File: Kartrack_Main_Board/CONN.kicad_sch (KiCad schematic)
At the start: 4 parts, among them J1 USB_C_Receptacle_USB2.0_14P

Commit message: schematic GPS
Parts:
- added JP1: SolderJumper_2_Open, symbol Jumper:SolderJumper_2_Open
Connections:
- net +3.3V: no longer A2.4 (3V3)
- net PC6 renamed PC6_TX
- net PC7 renamed PC7_RX
- net VDD: no longer names the net of A2.8 (VIN)
- net VDD: now also JP1.1 (A)
- new net VEXT_DISCO: JP1.2 (B)
- no-connect marks 4 -> 5
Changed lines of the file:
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@@
+	)
+	(no_connect
+		(at 191.77 66.04)
 	)
 	(no_connect
@@
 	(wire
 		(pts
-			(xy 186.69 57.15) (xy 186.69 66.04)
+			(xy 186.69 54.61) (xy 186.69 55.88)
 		)
 		(stroke
@@
 	(wire
 		(pts
+			(xy 186.69 63.5) (xy 186.69 66.04)
+		)
+		(stroke
+			(width 0)
+			(type default)
+		)
+	)
+	(wire
+		(pts
 			(xy 71.12 74.93) (xy 72.39 74.93)
 		)
@@
 	(wire
 		(pts
-			(xy 190.5 66.04) (xy 191.77 66.04)
-		)
-		(stroke
-			(width 0)
-			(type default)
-		)
-	)
-	(wire
-		(pts
 			(xy 71.12 80.01) (xy 77.47 80.01)
 		)
@@
 		)
 	)
-	(wire
-		(pts
-			(xy 190.5 66.04) (xy 190.5 63.5)
-		)
-		(stroke
-			(width 0)
-			(type default)
-		)
-	)
 	(hierarchical_label "PI1{slash}LD1"
 		(shape input)
@@
 		)
 	)
-	(hierarchical_label "PC6"
+	(hierarchical_label "PC6_TX"
 		(shape input)
 		(at 176.53 78.74 180)
@@
 		)
 	)
-	(hierarchical_label "PC7"
+	(hierarchical_label "PC7_RX"
 		(shape input)
 		(at 176.53 76.2 180)
@@
 	)
 	(symbol
-		(lib_id "power:+3.3V")
-		(at 190.5 63.5 0)
-		(unit 1)
-		(exclude_from_sim no)
-		(in_bom yes)
-		(on_board yes)
-		(dnp no)
-		(fields_autoplaced yes)
-		(property "Reference" "#PWR03"
-			(at 190.5 67.31 0)
-			(effects
-				(font
-					(size 1.27 1.27)
-				)
-				(hide yes)
-			)
-		)
-		(property "Value" "+3.3V"
-			(at 190.5 58.42 0)
-			(effects
-				(font
-					(size 1.27 1.27)
-				)
-			)
-		)
-		(property "Footprint" ""
-			(at 190.5 63.5 0)
-			(effects
-				(font
-					(size 1.27 1.27)
-				)
-				(hide yes)
-			)
-		)
-		(property "Datasheet" ""
-			(at 190.5 63.5 0)
-			(effects
-				(font
-					(size 1.27 1.27)
-				)
-				(hide yes)
-			)
-		)
-		(property "Description" "Power symbol creates a global label with name \"+3.3V\""
-			(at 190.5 63.5 0)
-			(effects
-				(font
-					(size 1.27 1.27)
-				)
-				(hide yes)
-			)
-		)
-		(pin "1"
-		)
-		(instances
-			(project "Kartrack_Main_Board"
-				(path "/7d0ecb76-dd3a-488e-b45e-ae217463e751/85ccdc23-ae17-49a7-b6f3-41d41d1b2e3d"
-					(reference "#PWR03")
-					(unit 1)
-				)
-			)
-		)
-	)
-	(symbol
 		(lib_id "power:VDD")
-		(at 186.69 57.15 0)
+		(at 186.69 54.61 0)
 		(unit 1)
 		(exclude_from_sim no)
@@
 		(fields_autoplaced yes)
 		(property "Reference" "#PWR04"
-			(at 186.69 60.96 0)
-			(effects
-				(font
-					(size 1.27 1.27)
-				)
-				(hide yes)
-			)
-		)
-		(property "Value" "VDD"
-			(at 186.69 52.07 0)
+			(at 186.69 58.42 0)
+			(effects
+				(font
+					(size 1.27 1.27)
+				)
+				(hide yes)
+			)
+		)
+		(property "Value" "VEXT_DISCO"
+			(at 186.69 49.53 0)
 			(effects
 				(font
@@
 		)
 		(property "Footprint" ""
-			(at 186.69 57.15 0)
+			(at 186.69 54.61 0)
 			(effects
 				(font
@@
 		)
 		(property "Datasheet" ""
-			(at 186.69 57.15 0)
+			(at 186.69 54.61 0)
 			(effects
 				(font
@@
 		)
 		(property "Description" "Power symbol creates a global label with name \"VDD\""
-			(at 186.69 57.15 0)
+			(at 186.69 54.61 0)
 			(effects
 				(font
@@
 					(unit 1)
 				)
+			)
+		)
+	)
+	(symbol
+		(lib_id "Jumper:SolderJumper_2_Open")
+		(at 186.69 59.69 90)
+		(unit 1)
+		(exclude_from_sim yes)
+		(in_bom no)
+		(on_board yes)
+		(dnp no)
+		(property "Reference" "JP1"
+			(at 173.736 57.912 90)
+			(effects
+				(font
+					(size 1.27 1.27)
+				)
+				(justify right)
+			)
+		)
+		(property "Value" "SolderJumper_2_Open"
+			(at 159.512 60.96 90)
+			(effects
+				(font
+					(size 1.27 1.27)
+				)
+				(justify right)
+			)
+		)
+		(property "Footprint" ""
+			(at 186.69 59.69 0)
+			(effects
+				(font
+					(size 1.27 1.27)
+				)
+				(hide yes)
+			)
+		)
+		(property "Datasheet" "~"
+			(at 186.69 59.69 0)
+			(effects
+				(font
+					(size 1.27 1.27)
+				)
+				(hide yes)
+			)
+		)
+		(property "Description" "Solder Jumper, 2-pole, open"
+			(at 186.69 59.69 0)
+			(effects
+				(font
+					(size 1.27 1.27)
+				)
+				(hide yes)
+			)
+		)
+		(pin "2"
+		)
+		(pin "1"
+		)
+		(instances
+			(project ""
+				(path "/7d0ecb76-dd3a-488e-b45e-ae217463e751/85ccdc23-ae17-49a7-b6f3-41d41d1b2e3d"
+					(reference "JP1")
+					(unit 1)
+				)

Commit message: BLOC schematic
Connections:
- net PB14 renamed PB14_SPI2_MISO
- net PB15 renamed PB15_SPI2_MOSI
- net PB8 renamed PB8_SCL
- net PB9 renamed PB9_SDA
- net PI1/LD1 renamed PI1_SPI2_SCK
- net PIO renamed PIO_SPI2_NSS
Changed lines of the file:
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@@
 		)
 	)
-	(hierarchical_label "PI1{slash}LD1"
+	(hierarchical_label "PI1_SPI2_SCK"
 		(shape input)
 		(at 176.53 109.22 180)
@@
 		)
 	)
-	(hierarchical_label "PB8"
+	(hierarchical_label "PB8_SCL"
 		(shape input)
 		(at 201.93 111.76 0)
@@
 		)
 	)
-	(hierarchical_label "PIO"
+	(hierarchical_label "PIO_SPI2_NSS"
 		(shape input)
 		(at 176.53 88.9 180)
@@
 		)
 	)
-	(hierarchical_label "PB15"
+	(hierarchical_label "PB15_SPI2_MOSI"
 		(shape input)
 		(at 176.53 104.14 180)
@@
 		)
 	)
-	(hierarchical_label "PB14"
+	(hierarchical_label "PB14_SPI2_MISO"
 		(shape input)
 		(at 176.53 106.68 180)
@@
 		)
 	)
-	(hierarchical_label "PB9"
+	(hierarchical_label "PB9_SDA"
 		(shape input)
 		(at 201.93 109.22 0)

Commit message: ajouts des boutons
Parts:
- added SW1, SW2, SW3: SW_Push, symbol Switch:SW_Push
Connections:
- net +3.3V: now also SW1.2, SW2.2, SW3.2
- net PA0: now also SW1.1
- net PF10: now also SW2.1
- net PF9: now also SW3.1

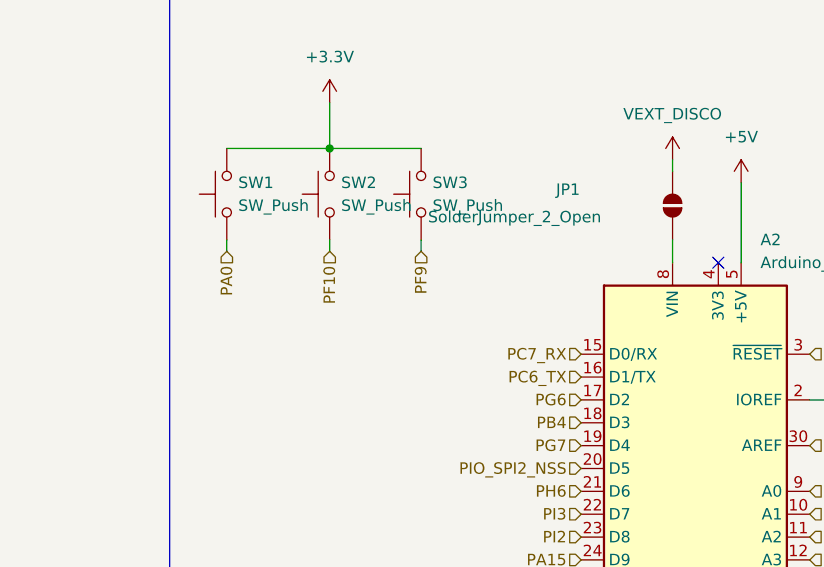
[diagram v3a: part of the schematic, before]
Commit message: added connectors for pulldown pushbuttons
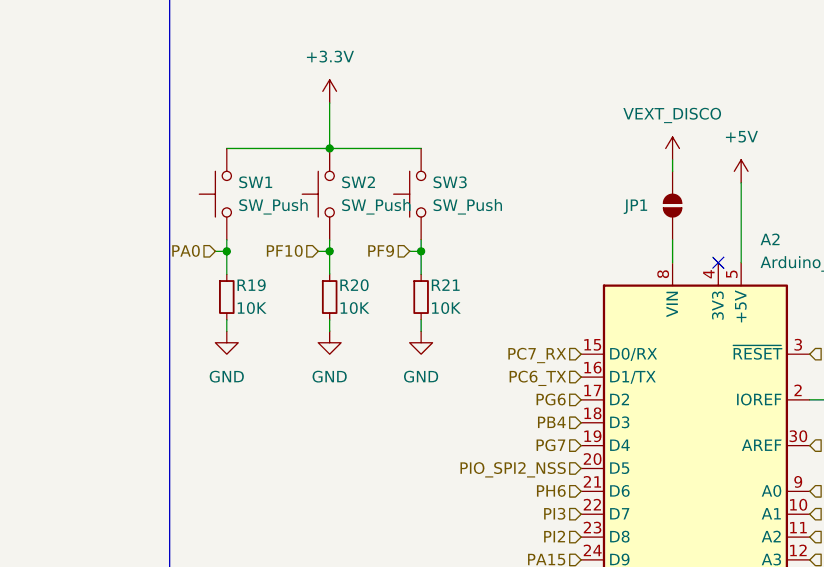
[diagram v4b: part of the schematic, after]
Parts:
- added R19, R20, R21: 10K, symbol Device:R_Small
- SW1, SW2, SW3: footprint (none) -> Connector_PinSocket_2.54mm:PinSocket_1x02_P2.54mm_Vertical_SMD_Pin1Left
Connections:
- net GND: now also R19.2, R20.2, R21.2
- net PA0: now also R19.1
- net PF10: now also R20.1
- net PF9: now also R21.1

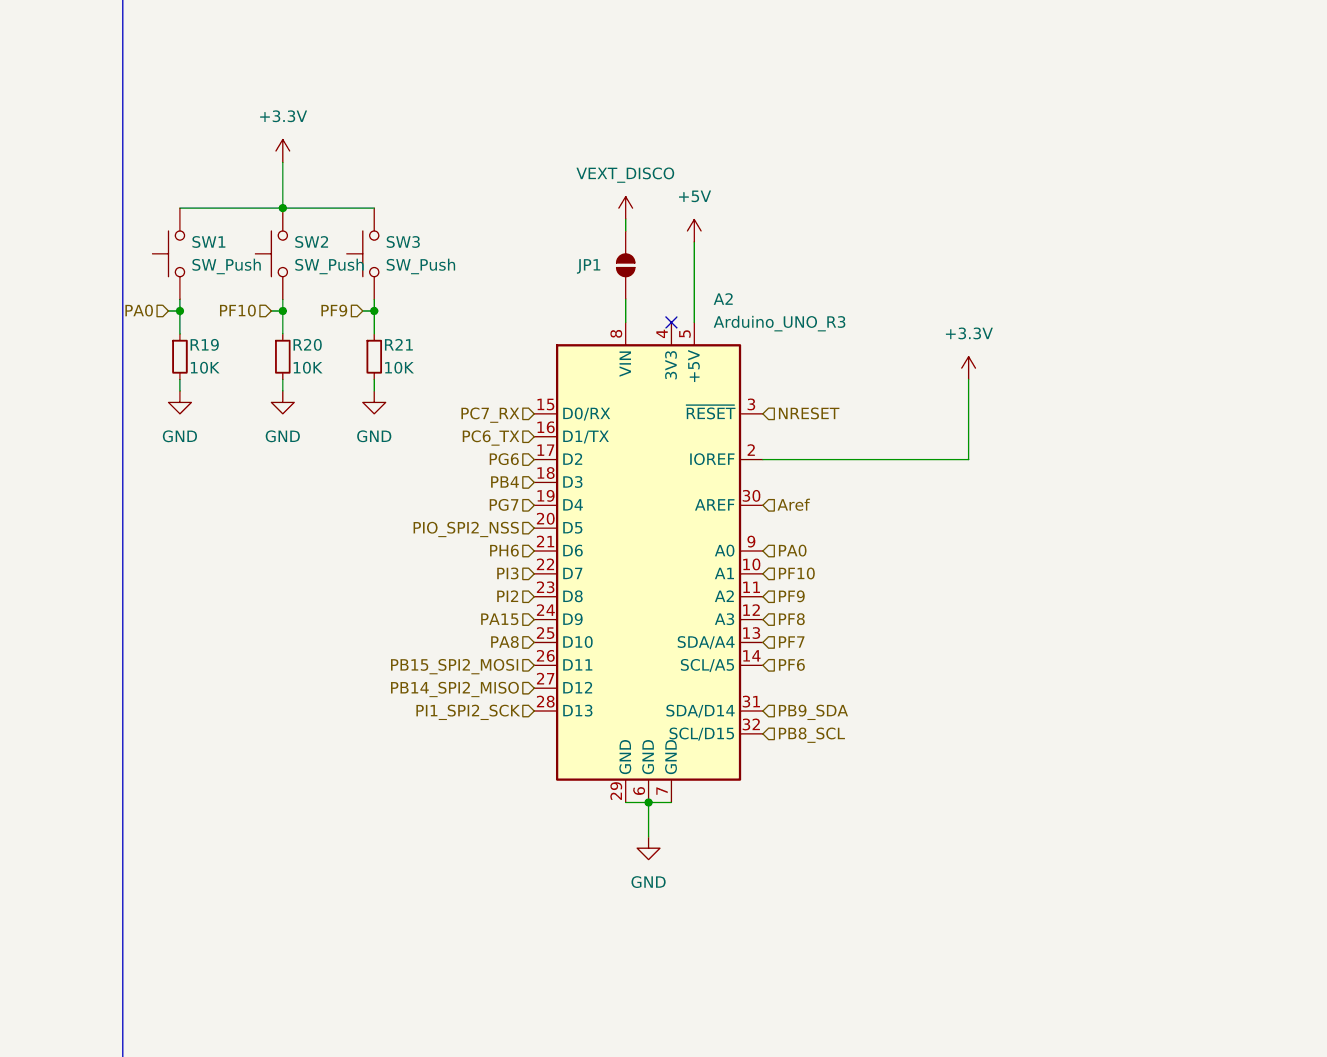
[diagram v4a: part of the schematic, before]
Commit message: add filtering button
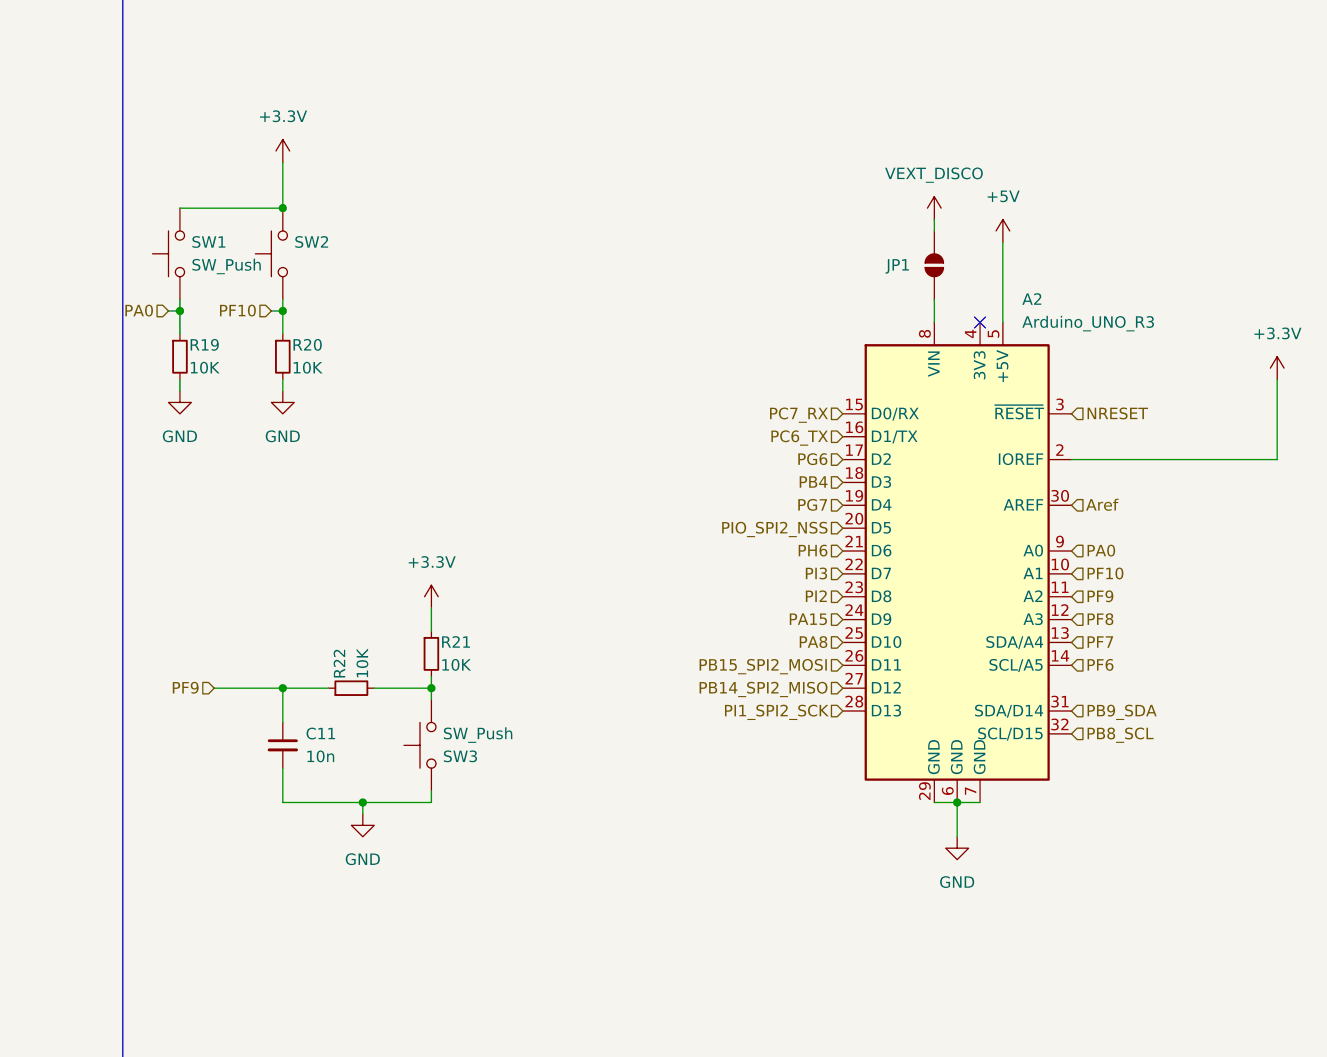
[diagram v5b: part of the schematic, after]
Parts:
- added C11: 10n, symbol Device:C_Small
- added R22: 10K, symbol Device:R_Small
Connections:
- net +3.3V: now also R21.1; no longer SW3.2
- net GND: now also SW3.2, C11.2; no longer R21.2
- net PF9: now also C11.1, R22.1; no longer R21.1, SW3.1
- new net: R21.2, R22.2, SW3.1
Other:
- moved on the sheet: A2, JP1, R21, SW3
